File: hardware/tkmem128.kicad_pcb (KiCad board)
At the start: 2 copper layers, 78.7 x 66 mm, 24 parts, among them J1 Para a expansora, U1 GAL20V8B, U2 74HCT273, U3 AS6C1008-55PCN, U4 27C256

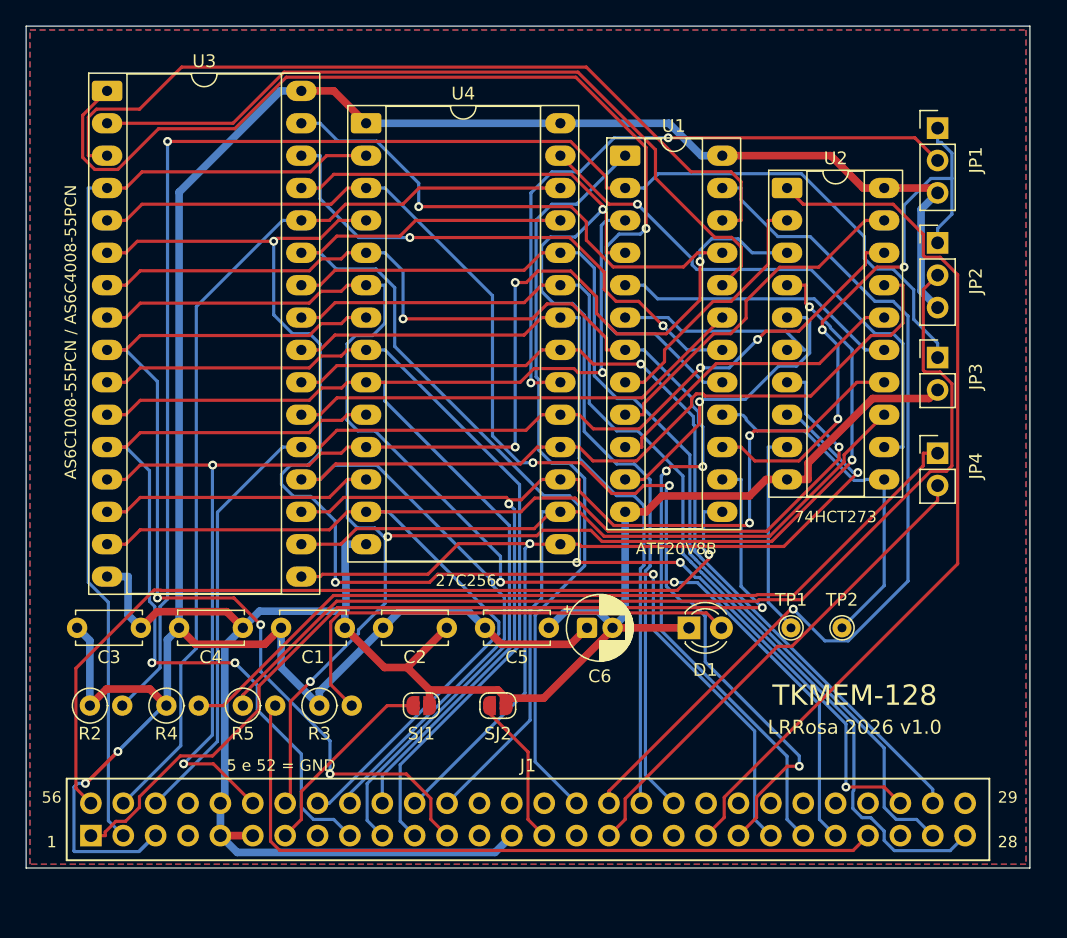
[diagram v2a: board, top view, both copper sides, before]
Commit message: Arquitetura corrigida: conector na placa principal, tira soldada nos terminais
As fotos do periferico de audio (mesma construcao da TKMEM) mostraram como o
conjunto realmente se monta, e o datasheet do TE 5645235 confirmou o porque:

  - o conector de borda e de ENTRADA VERTICAL, ou seja, o cartao entra
    perpendicular a placa que o segura. Por isso ele vai soldado direto na
    placa PRINCIPAL, que fica em pe: a fenda cai no plano horizontal e recebe
    o cartao do TK;
  - os terminais atravessam a placa principal e sobram 3,18 mm do outro lado;
  - a tira de expansao encosta nesses terminais e e soldada neles. Ela nao tem
    conector nenhum: 56 ilhas de solda de um lado, dedos de borda do outro.

Com isso a tira fica coplanar com o cartao do TK e com a fenda do conector, e
a corrente de perifericos nao ganha degrau nenhum - que era o ponto levantado
na revisao.

Mudancas:

  placa principal  J1 troca do header 2x28 para o footprint do conector de
                   borda (2,54 x 4,85 mm, furo 1,02). O esquematico NAO mudou
                   (mesmo simbolo, mesmas nets), entao o rearranjo manual foi
                   preservado; so o cobre foi refeito.
  tira de expansao redesenhada: J1 = ilhas de solda 2x28, J2 = dedos de borda,
                   C1 de desacoplamento. 45 mm de comprimento.
  footprints       soquete passa a ter as 56 posicoes (a guia 5/52 e um
                   pedacinho de PCB que o montador encaixa, o conector tem
                   contato em todas). Novo ZX_TK_Bus_SolderPads_56.

Documentada tambem a orientacao de montagem: o lado dos componentes da placa
principal fica virado para a tira de expansao, nunca para o conector - ao
contrario a placa esbarra no micro dentro da caixa.

ERC 0, DRC 0 e netlist conferida no a no nas duas placas (74 e 53 nets).

Co-Authored-By: Claude Opus 5 <noreply@anthropic.com>
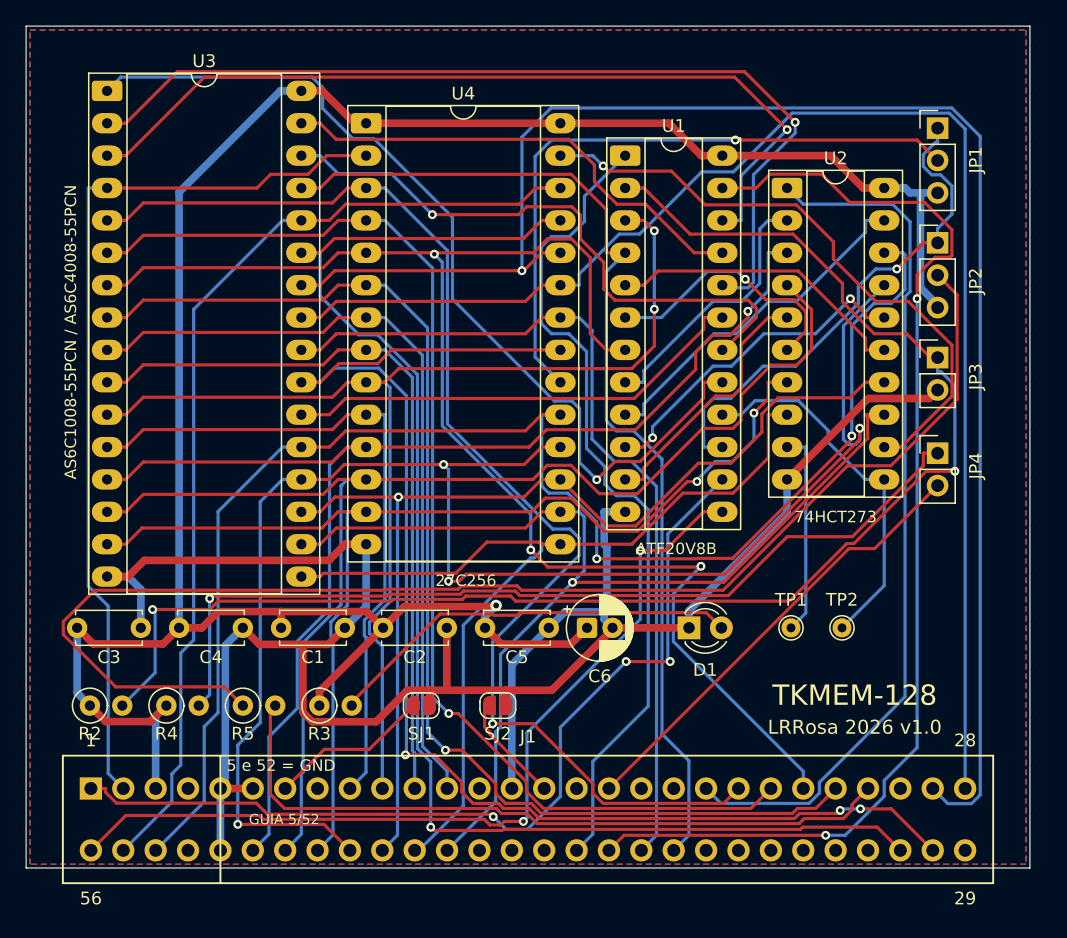
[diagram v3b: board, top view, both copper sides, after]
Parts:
- J1: value Para a expansora -> Barramento TK; footprint ZX_TK_Bus_Header_2x28 -> ZX_TK_Bus_Socket_56
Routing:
- net A9: track 81.7 -> 125.7 mm, vias 0 -> 1
- net A10: track 72.1 -> 104.6 mm, vias 1 -> 3
- net D7: track 87.0 -> 116.6 mm
- net A11: track 84.8 -> 111.5 mm
- net ROMCS_DRV: track 80.9 -> 105.3 mm
- net D6: track 100.2 -> 124.0 mm, vias 0 -> 4
- net IORQ_N: track 73.4 -> 91.0 mm, vias 1 -> 2
- net A3: track 78.4 -> 61.8 mm, vias 3 -> 0
- net A8: track 94.8 -> 110.0 mm, vias 3 -> 1
- net A5: track 97.5 -> 112.0 mm
- net D2: track 105.5 -> 91.8 mm, vias 1 -> 2
- net GND: track 157.9 -> 170.1 mm
- net A0: track 65.5 -> 53.4 mm, vias 2 -> 0
- net SA16: track 62.0 -> 73.9 mm, vias 0 -> 1
- net A6: track 104.6 -> 93.0 mm, vias 3 -> 1
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
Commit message: Conector no verso, sem furos na guia, tira soldada dos dois lados
Tres correcoes de revisao:

1. A guia ocupa a posicao das vias 5 e 52, entao nao ha terminal ali e a placa
   nao precisa de furo. Footprint do conector volta de 56 para 54 furos. O
   simbolo continua com 56 pinos, o que deixou o esquematico rearranjado a mao
   intacto - o KiCad aceita os dois pinos sem ilha e o DRC fica zerado (sao
   GND, que tem ilha de sobra).

2. A placa principal estava invertida em relacao ao conector. Ele e o UNICO
   componente do lado do cobre: entra por baixo e e soldado por cima, pelo lado
   dos componentes, que fica virado para a tira de expansao. J1 passa para a
   camada B.Cu. O espelhamento que vem junto e a consequencia fisica de enfiar
   a peca pelo outro lado, e reforca o teste de continuidade do item 2.

3. A tira nao encosta nos terminais por fora: os terminais sao RETOS e ficam em
   duas fileiras a 4,85 mm, entao a tira entra ENTRE elas - uma fileira por
   cima, outra por baixo - e e soldada dos DOIS LADOS. O footprint passa a ter
   ilhas nas duas faces (F.Cu = 29..56, B.Cu = 1..28), nao SMD de uma face so.

Roteamento refeito nas duas placas, ambas 100% fechadas em 2 camadas com
isolacao de 0,14 mm. ERC 0, DRC 0 erros, 0 desconexoes, netlist conferida no a
no (74 e 53 nets). A serigrafia ajustada a mao foi preservada.

Co-Authored-By: Claude Opus 5 <noreply@anthropic.com>
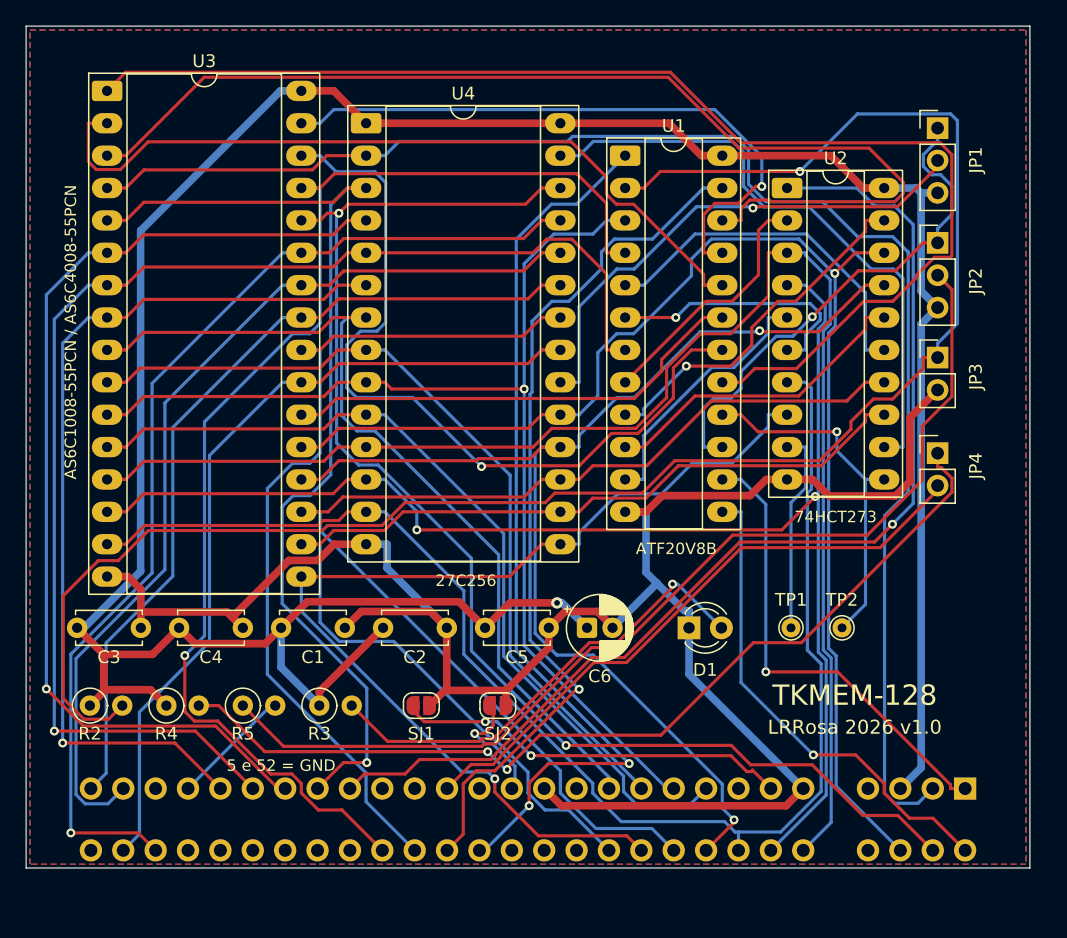
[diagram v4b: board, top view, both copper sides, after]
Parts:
- J1: moved to B.Cu
- turned J1 to 180 degrees
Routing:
- net A9: track 125.7 -> 74.0 mm, vias 1 -> 0
- net ROMCS_BUS: track 56.3 -> 9.53 mm
- net A12: track 71.1 -> 117.6 mm
- net A11: track 111.5 -> 66.0 mm
- net A10: track 104.6 -> 64.7 mm, vias 3 -> 0
- net +5V: track 186.4 -> 223.9 mm
- net A14: track 71.7 -> 37.0 mm, vias 3 -> 1
- net A15: track 68.2 -> 38.3 mm, vias 2 -> 1
- net D6: track 124.0 -> 94.8 mm, vias 4 -> 2
- net A8: track 110.0 -> 82.4 mm
- net SA18: track 72.9 -> 99.6 mm, vias 1 -> 0
- net A13: track 77.4 -> 103.7 mm, vias 0 -> 2
- net ROMCS_DRV: track 105.3 -> 80.8 mm
- net A4: track 95.2 -> 70.9 mm
- net IORQ_N: track 91.0 -> 68.5 mm, vias 2 -> 1
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
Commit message: Corrige a fileira dos pinos do conector: 1..28 embaixo
Eu tinha invertido as fileiras do footprint do conector de borda em relacao ao
que estava antes: os pinos 1..28 ficaram do lado de dentro da placa quando
devem ficar junto a aresta INFERIOR, que e a fileira de baixo do cartao do TK.
Corrigido no gerador do footprint.

Havia tambem um erro em troca_j1.py: ele lia a rotacao gravada na placa (que ja
carregava o efeito do flip anterior) e reaplicava rotacao + flip, espelhando
duas vezes. Agora o footprint e sempre reposicionado com rotacao 0 e so entao
flipado para B.Cu.

Convencao documentada no README e no item 2 de ANTES-DE-FABRICAR: com a placa
em pe e o conector na borda de baixo, 1..28 fica na fileira de baixo (pino 1 =
A14, junto a borda) e 29..56 na de cima.

Placa principal reroteada: 100% fechada em 2 camadas com isolacao de 0,14 mm.
ERC 0, DRC 0 erros, 0 desconexoes nas duas placas.

Co-Authored-By: Claude Opus 5 <noreply@anthropic.com>
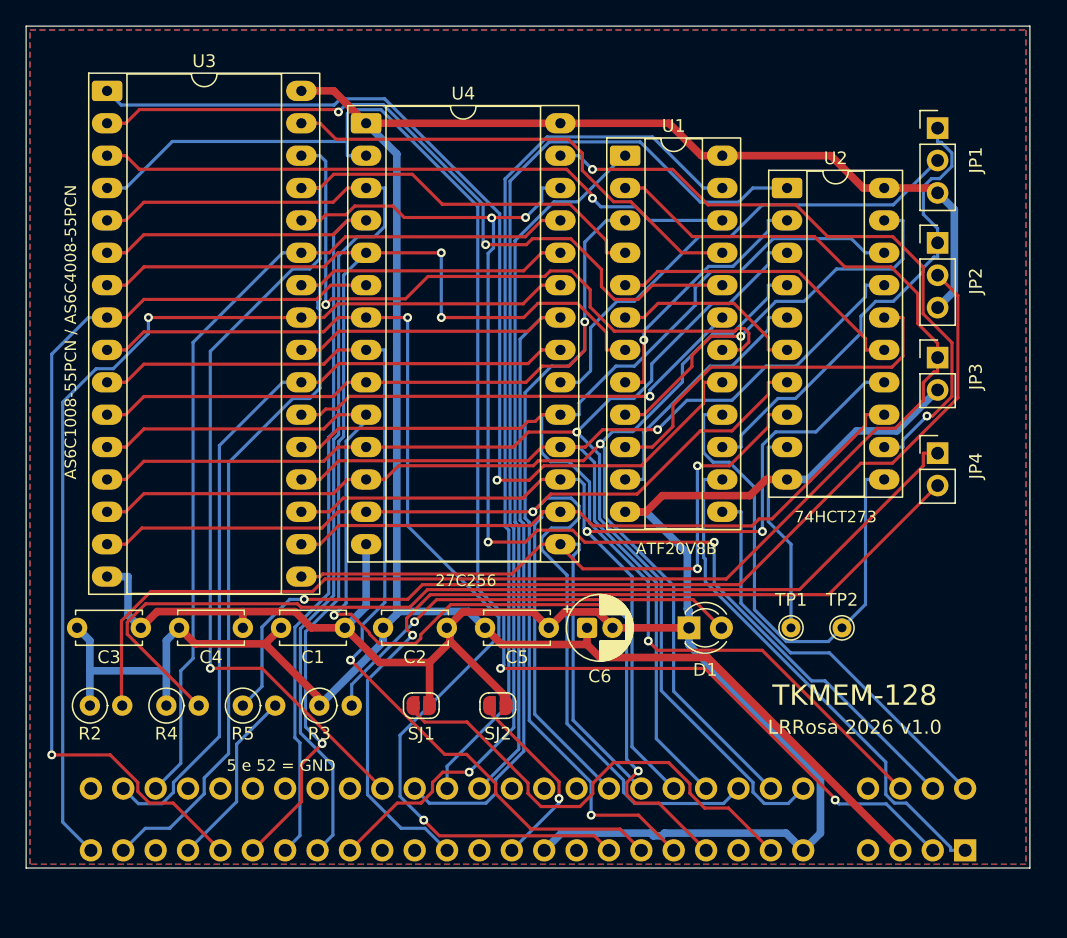
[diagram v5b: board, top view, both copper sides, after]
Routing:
- net SA14: track 85.0 -> 50.5 mm, vias 0 -> 1
- net +5V: track 223.9 -> 195.8 mm, vias 1 -> 0
- net ZX512: track 138.9 -> 112.7 mm, vias 1 -> 0
- net SA18: track 99.6 -> 78.0 mm, vias 0 -> 1
- net RAMDIS: track 48.5 -> 69.5 mm, vias 0 -> 1
- net A0: track 67.5 -> 86.4 mm, vias 0 -> 3
- net A3: track 69.5 -> 86.5 mm, vias 0 -> 2
- net MREQ_N: track 71.7 -> 55.7 mm, vias 2 -> 0
- net D1: track 109.1 -> 94.6 mm, vias 2 -> 1
- net D0: track 114.6 -> 100.8 mm, vias 0 -> 1
- net A11: track 66.0 -> 79.7 mm, vias 0 -> 1
- net A8: track 82.4 -> 69.0 mm, vias 1 -> 0
- net A1: track 89.7 -> 103.1 mm, vias 1 -> 2
- net CLK7FFD: track 28.1 -> 41.4 mm, vias 1 -> 0
- net SA15: track 50.4 -> 38.0 mm, vias 1 -> 0
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
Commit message: Serigrafia da tira: numeracao por face, nas duas faces
As ilhas de J1 e os dedos de J2 sao SMD — cada pino existe em UMA face so. Na
coluna x=73,66 o cobre de F.Cu e o pino 56 e o de B.Cu e o pino 1. A serigrafia
da frente de J1 estava escrita "1" e "28": nomeando os pads de tras. Vira
56 / 29. J2, do lado, ja estava certo, o que so deixava a divergencia mais
visivel na placa.

A tira e soldada dos DOIS lados, entao quem monta olha as duas faces. Cada face
passa a trazer a numeracao dos seus proprios pinos, em J1 e em J2:

  F.Silkscreen   29 ..... 56      (os pads de F.Cu)
  B.Silkscreen    1 ..... 28      (os pads de B.Cu)

Vem trocado de lado entre as faces porque e a mesma placa vista por tras.
"SOLDAR DOS DOIS LADOS" tambem passa a aparecer no verso, que e justamente onde
alguem pode nao perceber que ha o que soldar.

Contorno de J1 refeito: era um retangulo fechado, mas do lado das ilhas fica a
ARESTA da placa, entao um dos lados caia fora da placa e a marca da guia
atravessava a borda (3 avisos de silk_edge_clearance, agora duplicados ao levar
o desenho para o verso). Vira um U aberto para a aresta, parando 0,3 mm antes
dela, nas duas faces. DRC da tira: de 3 avisos para 0.

"PASSAGEM ->" era ambiguo: a flecha apontava para +x, mas os dedos ficam para
baixo. Vira "PARA OUTROS PERIFERICOS", centrado logo acima deles — a
proximidade ja diz a direcao, e o texto diz o que e.

confere_alinhamento.py ganhou a verificacao dessa classe de erro: para cada
rotulo numerico de serigrafia, acha o pad mais proximo NAQUELA face e exige que
o numero bata. Verificado com teste negativo (reintroduzir o erro faz o script
sair com codigo 1). Vale para as duas placas.

Inclui o rearranjo manual do Leonardo no esquematico e na serigrafia das duas
placas.

DRC 0 violacoes, 0 desconexoes. Alinhamento entre as placas inalterado.

Co-Authored-By: Claude Opus 5 <noreply@anthropic.com>
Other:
- board text removed: "5 e 52 = GND"
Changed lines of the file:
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@@
 		(tags "conector borda edge socket 56 ZX Spectrum TK90X TK95")
 		(property "Reference" "J1"
-			(at 0 6.5 0)
+			(at 0 6.23 0)
 			(layer "B.SilkS")
 			(effects
@@
 		)
 		(fp_text user "29"
-			(at 34.29 6.2 0)
+			(at 37.87 2.73 0)
 			(layer "B.SilkS")
 			(effects
@@
 		)
 		(fp_text user "28"
-			(at 34.29 -6.2 0)
+			(at 37.87 -2.27 0)
 			(layer "B.SilkS")
 			(effects
@@
 		)
 		(fp_text user "GUIA 5/52"
-			(at -19.13 0 0)
+			(at -24.13 5.73 0)
 			(layer "B.SilkS")
 			(effects
@@
 			)
 		)
-		(fp_text user "56"
-			(at -34.29 6.2 0)
+		(fp_text user "1"
+			(at -37.13 -2.27 0)
 			(layer "B.SilkS")
 			(effects
@@
 			)
 		)
-		(fp_text user "1"
-			(at -34.29 -6.2 0)
+		(fp_text user "56"
+			(at -37.63 2.73 0)
 			(layer "B.SilkS")
 			(effects
@@
 		(layer "Edge.Cuts")
 	)
-	(gr_text "5 e 52 = GND"
-		(at 20 58 0)
-		(layer "F.SilkS")
-		(effects
-			(font
-				(size 0.9 0.9)
-				(thickness 0.15)
-			)
-		)
-	)
 	(gr_text "27C256"
 		(at 34.5 43.5 0)
@@
 	)
 	(gr_text "Derivado de Velesoft 2009 e Luccas Eletrônica 2012"
-		(at 39.5 58 0)
+		(at 39.5 54 0)
 		(layer "B.SilkS")
 		(effects
@@
 	)
 	(gr_text "github.com/lrrosa/tkmem128-kicad"
-		(at 39.5 55 0)
+		(at 39.5 51.5 0)
 		(layer "B.SilkS")
 		(effects
@@
 	)
 	(gr_text "CERN-OHL-S v2"
-		(at 39.5 52 0)
-		(layer "B.SilkS")
-		(effects
+		(at 39.5 49 0)
+		(layer "B.SilkS")
+		(effects

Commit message: Numeracao do conector tambem no lado dos componentes da principal
J1 fica em B.Cu - e o unico componente do lado do cobre - e toda a serigrafia
dele morava so em B.Silkscreen, o lado onde o conector e soldado. Mas o lado
dos componentes e onde a TIRA DE EXPANSAO e soldada, nos mesmos terminais que
atravessam a placa: quem monta precisa da numeracao la tambem.

O conector e THT, entao cada pino existe nas duas faces na mesma coluna e os
mesmos rotulos valem para as duas, nas mesmas coordenadas. Muda so qual ponta
aparece a esquerda, porque e a mesma placa vista do outro lado.

De quebra, o contorno do corpo do conector descia ate y=67,23 numa placa de
66,04 mm: 1,19 mm de serigrafia fora da placa e dois tracos verticais cruzando
a aresta - os 3 avisos de silk_edge_clearance que a principal carregava. O
mesmo tratamento que a tira levou: U aberto para a aresta, parando 0,3 mm antes
dela. O contorno cheio continua correto na biblioteca, porque o corpo de um
conector de borda avanca mesmo alem da placa; aparar e decisao de placa, nao de
footprint.

DRC da principal: de 5 violacoes para 2. As duas que sobram sao starved_thermal
nos pads de GND de C4 e C6, anteriores a isto e de outra natureza.

confere_alinhamento.py ja cobre a placa principal na verificacao de rotulos, e
segue passando nas duas.

Co-Authored-By: Claude Opus 5 <noreply@anthropic.com>
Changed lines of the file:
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@@
 		(fp_line
 			(start 36.49 5)
-			(end 36.49 -5)
+			(end 36.49 -3.51)
 			(stroke
 				(width 0.15)
-				(type solid)
+				(type default)
 			)
-			(layer "B.SilkS")
+			(layer "F.SilkS")
 		)
 		(fp_line
-			(start 36.49 -5)
-			(end -36.49 -5)
+			(start -24.13 5)
+			(end -24.13 -3.51)
 			(stroke
 				(width 0.15)
-				(type solid)
+				(type default)
+			)
+			(layer "F.SilkS")
+		)
+		(fp_line
+			(start -36.49 5)
+			(end 36.49 5)
+			(stroke
+				(width 0.15)
+				(type default)
+			)
+			(layer "F.SilkS")
+		)
+		(fp_line
+			(start -36.49 -3.51)
+			(end -36.49 5)
+			(stroke
+				(width 0.15)
+				(type default)
+			)
+			(layer "F.SilkS")
+		)
+		(fp_line
+			(start 36.49 5)
+			(end 36.49 -3.51)
+			(stroke
+				(width 0.15)
+				(type default)
 			)
 			(layer "B.SilkS")
@@
 		(fp_line
 			(start -24.13 5)
-			(end -24.13 -5)
+			(end -24.13 -3.51)
 			(stroke
 				(width 0.15)
-				(type solid)
+				(type default)
 			)
 			(layer "B.SilkS")
@@
 			(stroke
 				(width 0.15)
-				(type solid)
+				(type default)
 			)
 			(layer "B.SilkS")
 		)
 		(fp_line
-			(start -36.49 -5)
+			(start -36.49 -3.51)
 			(end -36.49 5)
 			(stroke
 				(width 0.15)
-				(type solid)
+				(type default)
 			)
 			(layer "B.SilkS")
@@
 		)
 		(fp_text user "29"
+			(at 37.87 2.73 0)
+			(layer "F.SilkS")
+			(effects
+				(font
+					(size 1 1)
+					(thickness 0.15)
+				)
+			)
+		)
+		(fp_text user "28"
+			(at 37.87 -2.27 0)
+			(layer "F.SilkS")
+			(effects
+				(font
+					(size 1 1)
+					(thickness 0.15)
+				)
+			)
+		)
+		(fp_text user "GUIA 5/52"
+			(at -24.13 5.73 0)
+			(layer "F.SilkS")
+			(effects
+				(font
+					(size 0.8 0.8)
+					(thickness 0.15)
+				)
+			)
+		)
+		(fp_text user "1"
+			(at -37.13 -2.27 0)
+			(layer "F.SilkS")
+			(effects
+				(font
+					(size 1 1)
+					(thickness 0.15)
+				)
+			)
+		)
+		(fp_text user "56"
+			(at -37.63 2.73 0)
+			(layer "F.SilkS")
+			(effects
+				(font
+					(size 1 1)
+					(thickness 0.15)
+				)
+			)
+		)
+		(fp_text user "29"
